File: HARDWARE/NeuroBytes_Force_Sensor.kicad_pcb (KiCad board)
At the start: 2 copper layers, 54 x 19 mm, 22 parts, among them P12 CONN_01X07, P6 CONN_01X04, P7 CONN_01X04, Q1 NPN_dual, Q2 NPN_dual, SW1 SW_PUSH, U1 STM32L011Gx, U2 LD3985G33R

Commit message: Updated PCB design files. Generated paste Gerber for stencil.
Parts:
- moved SW1 1.70 mm to (131.8, 88.7)
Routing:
- net GND: track 4.70 -> 11.7 mm
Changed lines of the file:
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@@
 (kicad_pcb (version 4) (host pcbnew 4.0.5-e0-6337~49~ubuntu14.04.1)
   (general
-    (links 76)
-    (no_connects 0)
-    (area 90.449999 71.449999 144.550001 90.550001)
+    (links 77)
+    (no_connects 4)
+    (area 86.9 62.899999 148.299752 94.049752)
     (thickness 1.6)
     (drawings 19)
-    (tracks 218)
+    (tracks 219)
     (zones 0)
     (modules 22)
@@
   )
   (setup
-    (last_trace_width 0.2)
+    (last_trace_width 1)
     (user_trace_width 0.5)
+    (user_trace_width 1)
     (trace_clearance 0.2)
     (zone_clearance 0.2)
@@
     (visible_elements FFFFFF7F)
     (pcbplotparams
-      (layerselection 0x00030_80000001)
+      (layerselection 0x00004_00000000)
       (usegerberextensions false)
       (excludeedgelayer true)
@@
       (outputformat 1)
       (mirror false)
-      (drillshape 1)
+      (drillshape 0)
       (scaleselection 1)
       (outputdirectory ""))
@@
     (add_net SWDIO/SCK)
   )
+  (module KiCad_Footprints:ZF_SW_Momentary_SideMtg (layer B.Cu)
+    (at 131.75 88.7 180)
+    (attr smd)
+    (fp_text reference SW1 (at -0.1 -1.65 180) (layer F.Fab)
+      (effects (font (size 1 1) (thickness 0.15)))
+    )
+    (fp_text value SW_PUSH (at 0 4.25 180) (layer B.Fab) hide
+      (effects (font (size 1 1) (thickness 0.15)) (justify mirror))
+    )
+    (fp_line (start 3.5 -1.7) (end 3.5 0.8) (layer B.SilkS) (width 0.15))
+    (fp_line (start 3.5 0.8) (end -3.5 0.8) (layer B.SilkS) (width 0.15))
+    (fp_line (start -3.5 0.8) (end -3.5 -1.7) (layer B.SilkS) (width 0.15))
+    (fp_line (start -3.5 -1.7) (end 3.5 -1.7) (layer B.SilkS) (width 0.15))
+    (pad 1 smd rect (at -2.1 0.95 180) (size 1 1.4) (layers B.Cu B.Paste B.Mask)
+      (net 2 GND))
+    (pad 2 smd rect (at 2.1 0.95 180) (size 1 1.4) (layers B.Cu B.Paste B.Mask)
+      (net 23 IDENTIFY))
+    (pad "" smd rect (at -3.5 -1.2 180) (size 2 1) (layers B.Cu B.Paste B.Mask)
+      (net 2 GND))
+    (pad "" smd rect (at 3.5 -1.2 180) (size 2 1) (layers B.Cu B.Paste B.Mask)
+      (net 2 GND))
+  )
   (module KiCad_Footprints:ZF_LED_RGB_SunLED_XZMDKCBDDG45S-9_cast (layer B.Cu)
     (at 129.875 76.4)
@@
     (pad 22 smd trapezoid (at -2 1.5 270) (size 0.3 0.5) (rect_delta 0.3 0 ) (layers B.Cu B.Paste B.Mask)
       (net 9 SWCLK/MISO))
-  )
-  (module KiCad_Footprints:ZF_SW_Momentary_SideMtg (layer B.Cu)
-    (at 131.75 90.4 180)
-    (fp_text reference SW1 (at 0 -1 180) (layer B.Fab)
-      (effects (font (size 1 1) (thickness 0.15)) (justify mirror))
-    )
-    (fp_text value SW_PUSH (at 0 4.25 180) (layer B.Fab) hide
-      (effects (font (size 1 1) (thickness 0.15)) (justify mirror))
-    )
-    (fp_line (start 3.5 0) (end 3.5 2.5) (layer B.SilkS) (width 0.15))
-    (fp_line (start 3.5 2.5) (end -3.5 2.5) (layer B.SilkS) (width 0.15))
-    (fp_line (start -3.5 2.5) (end -3.5 0) (layer B.SilkS) (width 0.15))
-    (fp_line (start -3.5 0) (end 3.5 0) (layer B.SilkS) (width 0.15))
-    (pad "" smd rect (at 0 0.5 180) (size 9 1) (layers B.Cu B.Paste B.Mask)
-      (net 2 GND))
-    (pad 1 smd rect (at -2.1 2.65 180) (size 1 1.4) (layers B.Cu B.Paste B.Mask)
-      (net 2 GND))
-    (pad 2 smd rect (at 2.1 2.65 180) (size 1 1.4) (layers B.Cu B.Paste B.Mask)
-      (net 23 IDENTIFY))
   )
   (module KiCad_Footprints:ZF_RN_4iso_CTS-0804 (layer B.Cu)
@@
   (segment (start 100.9 74) (end 101.5 74) (width 0.5) (layer B.Cu) (net 1))
   (segment (start 97.65 77.25) (end 100.9 74) (width 0.5) (layer B.Cu) (net 1))
+  (segment (start 128.25 89.9) (end 135.25 89.9) (width 1) (layer B.Cu) (net 2))
   (segment (start 139.375736 81.2) (end 139 81.2) (width 0.5) (layer F.Cu) (net 2))
   (segment (start 140.2 81.6) (end 139.775736 81.6) (width 0.5) (layer F.Cu) (net 2))

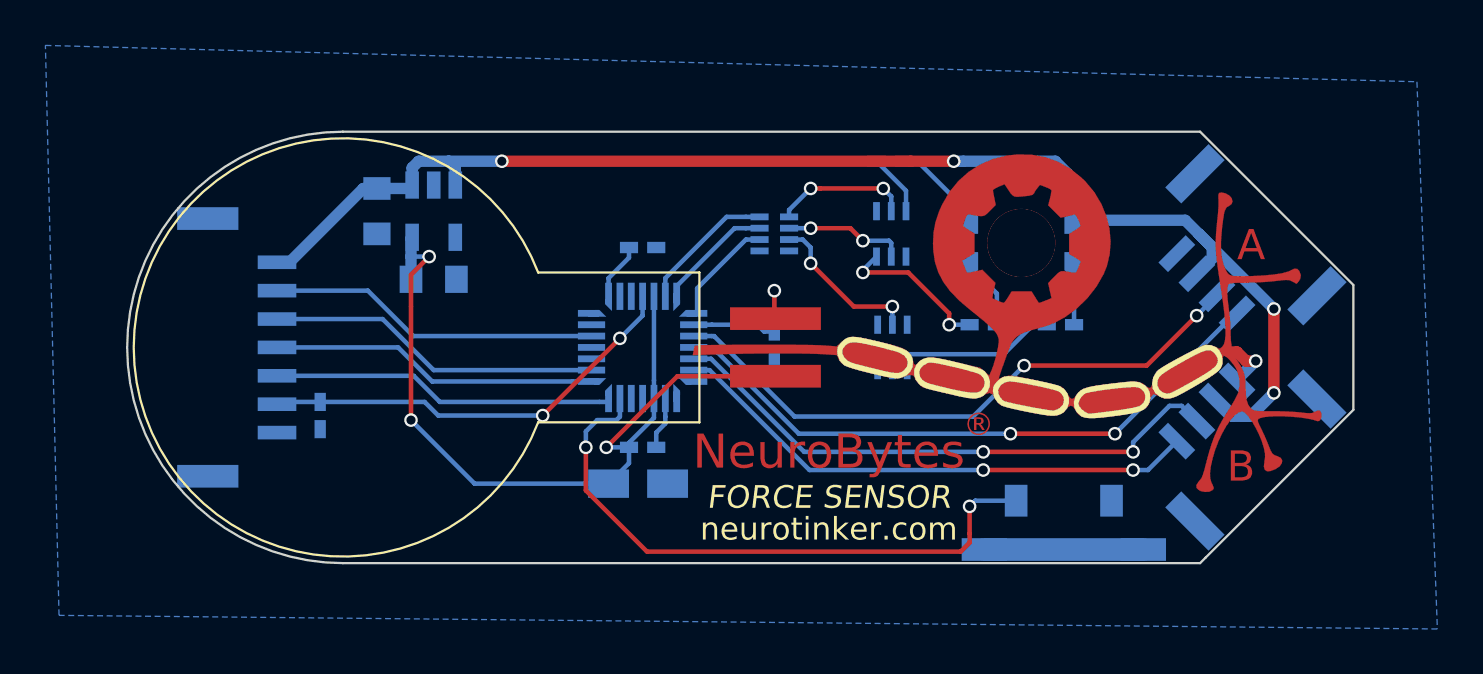
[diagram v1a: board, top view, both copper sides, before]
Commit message: updated power connector to 5-pin JST GH. minor routing/labeling changes.
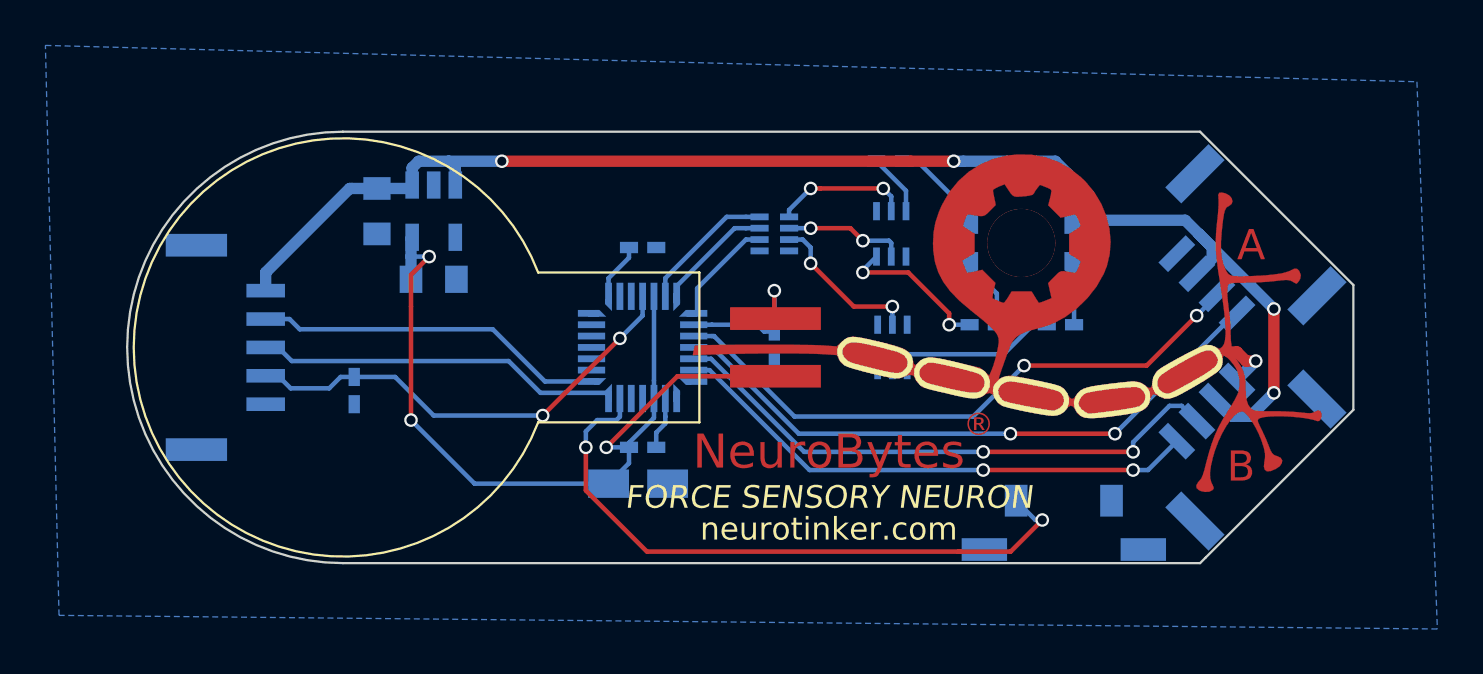
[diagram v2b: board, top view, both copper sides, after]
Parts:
- removed P12: CONN_01X07, KiCad_Footprints:ZF_CONN_JST_GH_7POS
- added P1: JST_GH_5-pos, KiCad_Footprints:ZF_CONN_JST_GH_5POS, B.Cu at (95.0, 81.0)
- moved C5 1.86 mm to (100.5, 82.9)
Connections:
- RN1 pad 1: LED_R -> LED_G
- RN1 pad 2: LED_G -> LED_R
- U1 pad 21: SWDIO/SCK -> SWDIO
- U1 pad 22: SWCLK/MISO -> SWCLK
- U1 pad 23: NSS -> Net-(U1-Pad23)
- U1 pad 26: MOSI -> Net-(U1-Pad26)
- U1 pad 6: LED_R -> LED_G
- U1 pad 7: LED_G -> LED_R
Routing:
- net SWDIO: track 0.00 -> 15.9 mm
- net SWCLK: track 0.00 -> 15.7 mm
- net MOSI: track 15.3 -> 0.00 mm
- net SWDIO/SCK: track 15.0 -> 0.00 mm
- net NSS: track 14.7 -> 0.00 mm
- net SWCLK/MISO: track 14.3 -> 0.00 mm
- net GND: track 11.7 -> 4.84 mm
- net +5V: track 59.9 -> 61.4 mm
- net IDENTIFY: track 27.1 -> 28.6 mm
- net RESET: track 19.2 -> 20.5 mm
- net LED_R: track 6.07 -> 5.01 mm
- net LED_G: track 5.01 -> 6.07 mm
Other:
- board text added: "FORCE SENSORY NEURON"
- board text removed: "FORCE SENSOR"

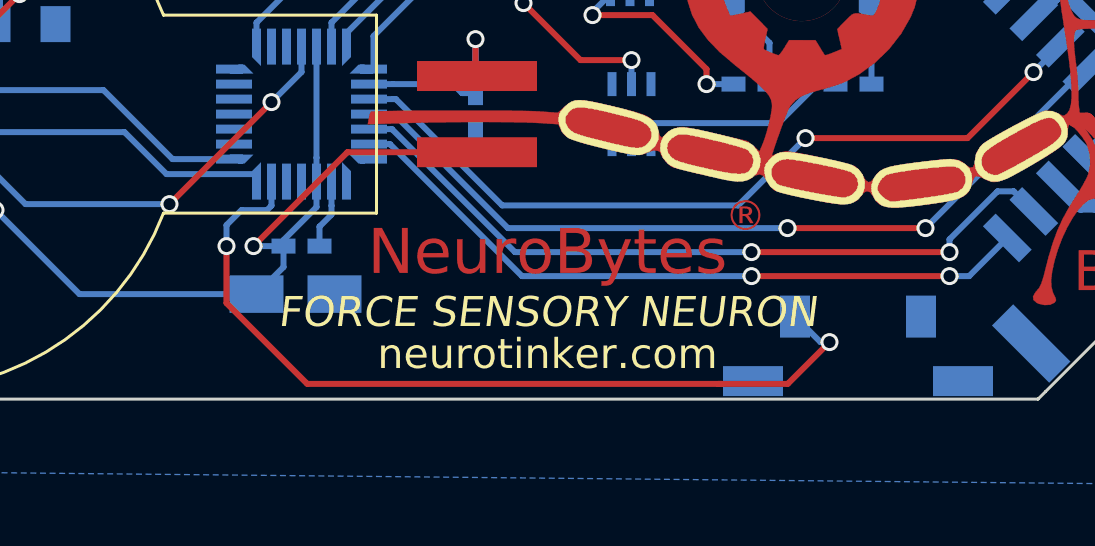
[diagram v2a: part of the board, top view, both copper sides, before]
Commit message: changed to Pressure Sensory Neuron
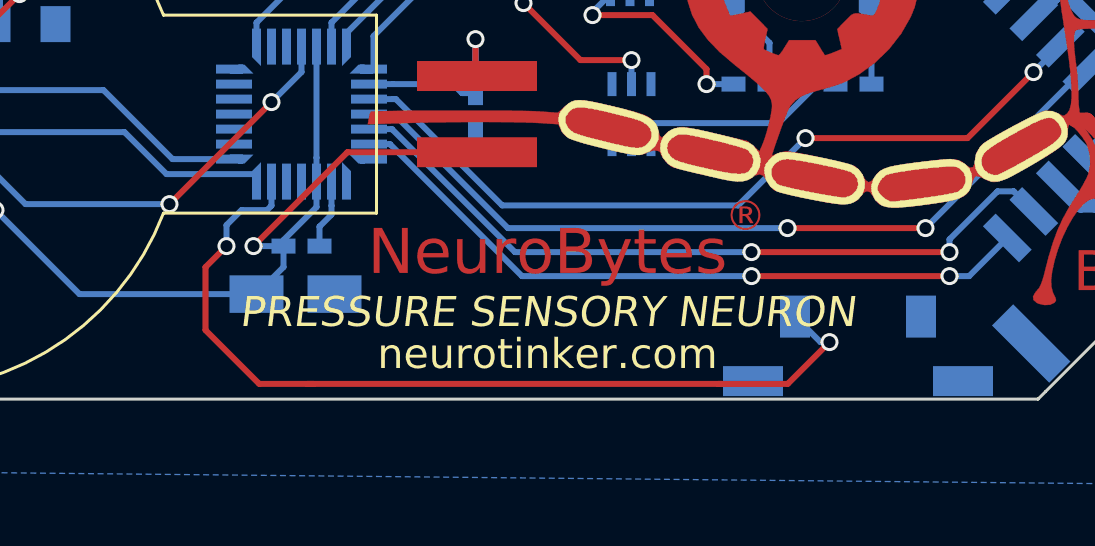
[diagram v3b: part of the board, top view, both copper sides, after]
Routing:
- net IDENTIFY: track 28.6 -> 30.3 mm
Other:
- board text added: "PRESSURE SENSORY NEURON"
- board text removed: "FORCE SENSORY NEURON"
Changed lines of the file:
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@@
-(kicad_pcb (version 4) (host pcbnew 4.0.5-e0-6337~49~ubuntu14.04.1)
+(kicad_pcb (version 4) (host pcbnew 4.0.7-e1-6374~58~ubuntu14.04.1)
   (general
     (links 75)
     (no_connects 0)
-    (area 90.449999 71.449999 144.550001 90.550001)
+    (area 86.9 62.899999 148.299752 94.049752)
     (thickness 1.6)
     (drawings 19)
-    (tracks 217)
+    (tracks 220)
     (zones 0)
     (modules 22)
@@
   )
   (setup
-    (last_trace_width 1)
+    (last_trace_width 0.2)
     (user_trace_width 0.5)
     (user_trace_width 1)
@@
   )
   (gr_line (start 126.5 63) (end 126.5 91) (layer Cmts.User) (width 0.2))
-  (gr_text "FORCE SENSORY NEURON" (at 121.4 87.6) (layer F.SilkS)
+  (gr_text "PRESSURE SENSORY NEURON" (at 121.4 87.6) (layer F.SilkS)
     (effects (font (size 1 1) (thickness 0.14) italic))
   )
@@
   (segment (start 116.9 75.25) (end 117.75 75.25) (width 0.2) (layer B.Cu) (net 18))
   (segment (start 117.75 75.25) (end 118.35 75.25) (width 0.2) (layer B.Cu) (net 18))
+  (segment (start 113.392596 89.992596) (end 113.6 89.992596) (width 0.2) (layer F.Cu) (net 19))
+  (segment (start 113.6 89.992596) (end 127.1 89.992596) (width 0.2) (layer F.Cu) (net 19))
+  (segment (start 110 88.2) (end 111.792596 89.992596) (width 0.2) (layer F.Cu) (net 19))
+  (segment (start 111.792596 89.992596) (end 113.6 89.992596) (width 0.2) (layer F.Cu) (net 19))
+  (segment (start 110 86.1) (end 110 88.2) (width 0.2) (layer F.Cu) (net 19))
+  (segment (start 110.7 85.4) (end 110 86.1) (width 0.2) (layer F.Cu) (net 19))
   (segment (start 130.8 88.6) (end 130.5 88.6) (width 0.2) (layer B.Cu) (net 19))
   (segment (start 130.5 88.6) (end 129.65 87.75) (width 0.2) (layer B.Cu) (net 19))
   (segment (start 127.1 89.992596) (end 127.207404 89.992596) (width 0.2) (layer F.Cu) (net 19))
-  (segment (start 113.392596 89.992596) (end 127.1 89.992596) (width 0.2) (layer F.Cu) (net 19))
   (via (at 130.8 88.6) (size 0.6) (drill 0.4) (layers F.Cu B.Cu) (net 19))
   (segment (start 127.1 89.992596) (end 129.407404 89.992596) (width 0.2) (layer F.Cu) (net 19))
   (segment (start 129.407404 89.992596) (end 130.8 88.6) (width 0.2) (layer F.Cu) (net 19))
-  (segment (start 110.7 85.4) (end 110.7 87.3) (width 0.2) (layer F.Cu) (net 19))
-  (segment (start 110.7 87.3) (end 113.392596 89.992596) (width 0.2) (layer F.Cu) (net 19))
   (segment (start 111.2 84.2) (end 110.7 84.7) (width 0.2) (layer B.Cu) (net 19))
   (segment (start 110.7 84.7) (end 110.7 85.4) (width 0.2) (layer B.Cu) (net 19))
